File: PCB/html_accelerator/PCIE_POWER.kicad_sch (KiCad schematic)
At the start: 1 part, among them U1 MCS9990

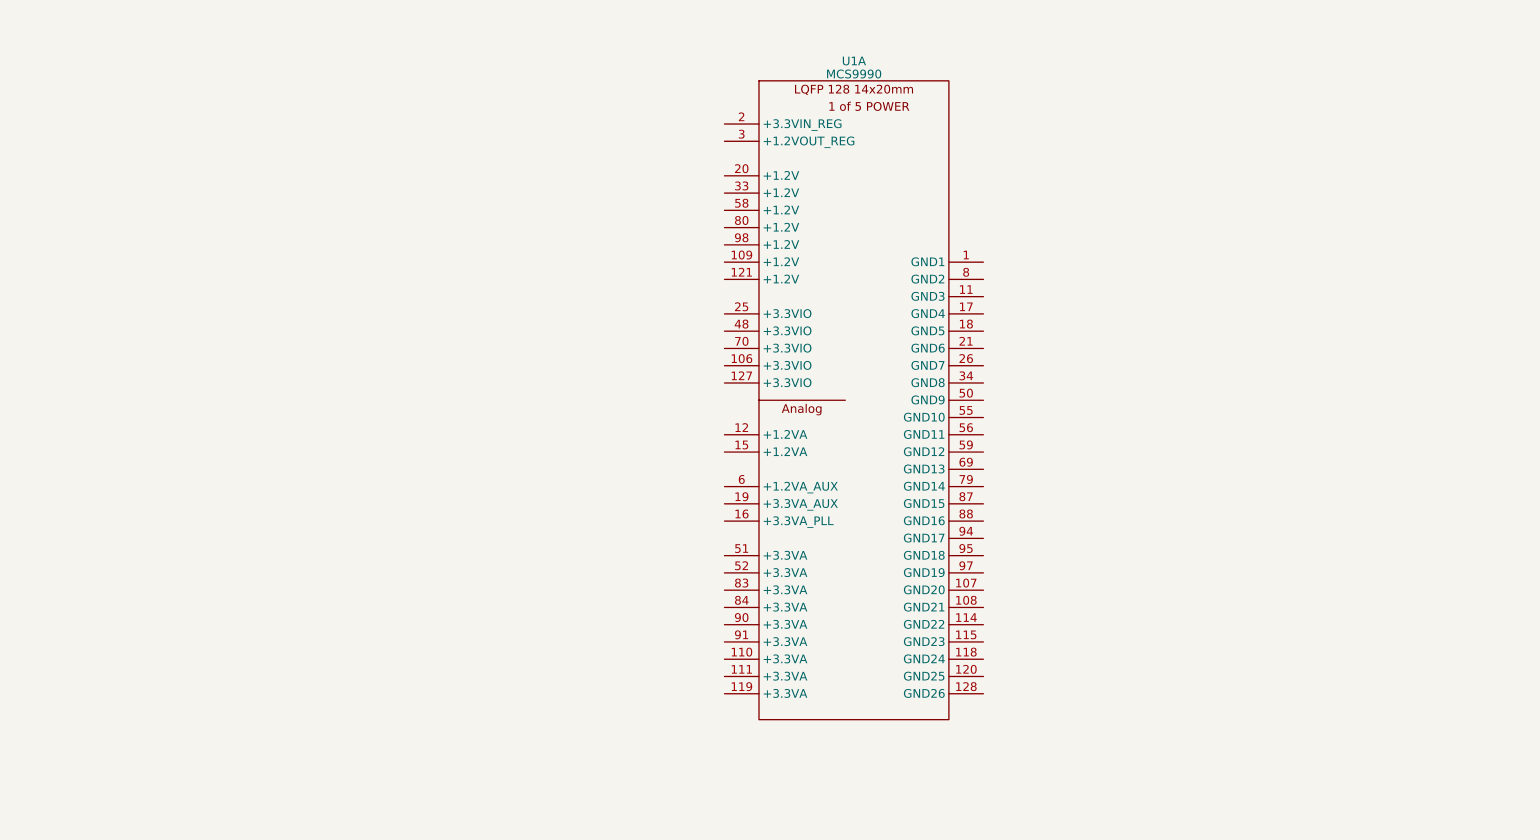
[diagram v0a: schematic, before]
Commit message: block diagram, datasheet updates
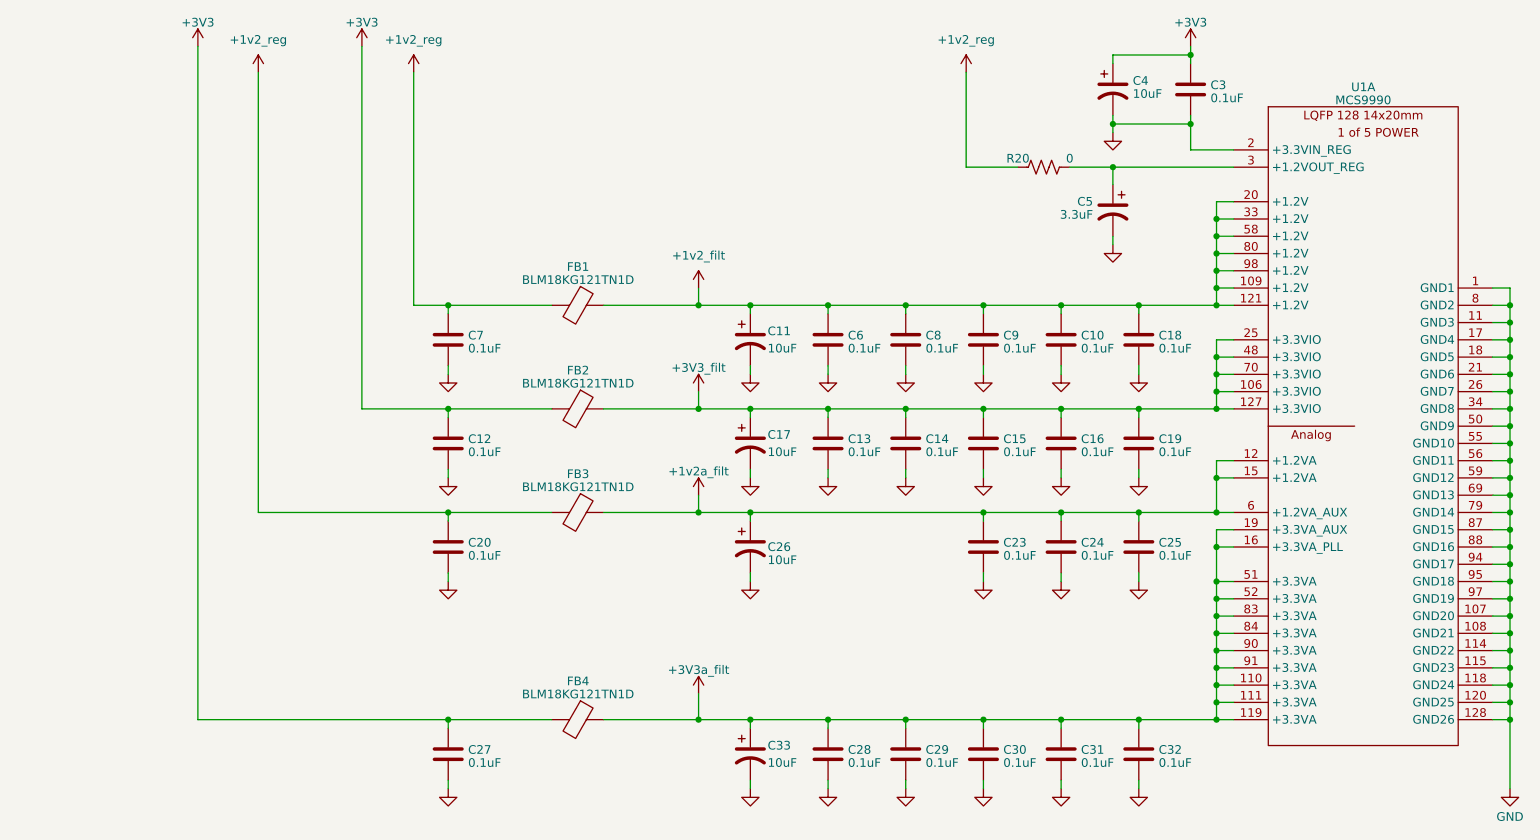
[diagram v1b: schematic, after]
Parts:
- added C10, C12, C13, C14, C15, C16, C18, C19, C20, C23, C24, C25, C27, C28, C29, C3, C30, C31, C32, C6, C7, C8, C9: 0.1uF, symbol Device:C
- added C11, C17, C26, C33, C4: 10uF, symbol Device:C_Polarized_US
- added C5: 3.3uF, symbol Device:C_Polarized_US
- added FB1, FB2, FB3, FB4: BLM18KG121TN1D, symbol Device:FerriteBead
- added R20: 0, symbol Device:R_US
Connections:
- net GND: now reaches U1.1 (GND1)
- net GND: now also U1.107 (GND20), U1.108 (GND21), U1.11 (GND3), U1.114 (GND22), U1.115 (GND23), U1.118 (GND24), U1.120 (GND25), U1.128 (GND26), U1.17 (GND4), U1.18 (GND5), U1.2 (+3.3VIN_REG), U1.21 (GND6), U1.26 (GND7), U1.34 (GND8), U1.50 (GND9), U1.55 (GND10), U1.56 (GND11), U1.59 (GND12), U1.69 (GND13), U1.79 (GND14), U1.8 (GND2), U1.87 (GND15), U1.88 (GND16), U1.94 (GND17), U1.95 (GND18), U1.97 (GND19), C10.2, C11.2, C12.2, C13.2, C14.2, C15.2, C16.2, C17.2, C18.2, C19.2, C20.2, C23.2, C24.2, C25.2, C26.2, C27.2, C28.2, C29.2, C3.2, C30.2, C31.2, C32.2, C33.2, C4.2, C5.2, C6.2, C7.2, C8.2, C9.2
- net +3V3: now reaches U1.106 (+3.3VIO)
- net +3V3: now also U1.109 (+1.2V), U1.110 (+3.3VA), U1.111 (+3.3VA), U1.119 (+3.3VA), U1.12 (+1.2VA), U1.121 (+1.2V), U1.127 (+3.3VIO), U1.15 (+1.2VA), U1.16 (+3.3VA_PLL), U1.19 (+3.3VA_AUX), U1.20 (+1.2V), U1.25 (+3.3VIO), U1.33 (+1.2V), U1.48 (+3.3VIO), U1.51 (+3.3VA), U1.52 (+3.3VA), U1.58 (+1.2V), U1.6 (+1.2VA_AUX), U1.70 (+3.3VIO), U1.80 (+1.2V), U1.83 (+3.3VA), U1.84 (+3.3VA), U1.90 (+3.3VA), U1.91 (+3.3VA), U1.98 (+1.2V), C10.1, C11.1, C12.1, C13.1, C14.1, C15.1, C16.1, C17.1, C18.1, C19.1, C20.1, C23.1, C24.1, C25.1, C26.1, C27.1, C28.1, C29.1, C3.1, C30.1, C31.1, C32.1, C33.1, C4.1, C6.1, C7.1, C8.1, C9.1, FB1.1, FB1.2, FB2.1, FB2.2, FB3.1, FB3.2, FB4.1, FB4.2, R20.1
- net at U1.3 (+1.2VOUT_REG): now also C5.1, R20.2
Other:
- moved on the sheet: U1A

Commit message: schematic updates
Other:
- title: (none) -> 12v, 3v3, 1v2 Power, Buck
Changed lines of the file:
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@@
 (kicad_sch (version 20230121) (generator eeschema)
   (paper "A4")
+  (title_block
+    (title "12v, 3v3, 1v2 Power, Buck")
+    (date "2024-09-15")
+    (rev "1")
+  )
   (junction (at 130.81 87.63) (diameter 0) (color 0 0 0 0)
   )
@@
   (symbol (lib_id "html_accel_Symbols:MCS9990") (at 207.01 43.18 0) (unit 1)
     (in_bom yes) (on_board yes) (dnp no) (fields_autoplaced)
-    (property "Reference" "U1" (at 220.98 40.2971 0)
-      (effects (font (size 1.27 1.27)))
+    (property "Reference" "U1" (at 220.98 38.8806 0)
+      (effects (font (size 3 3) bold))
     )
     (property "Value" "MCS9990" (at 220.98 42.2181 0)

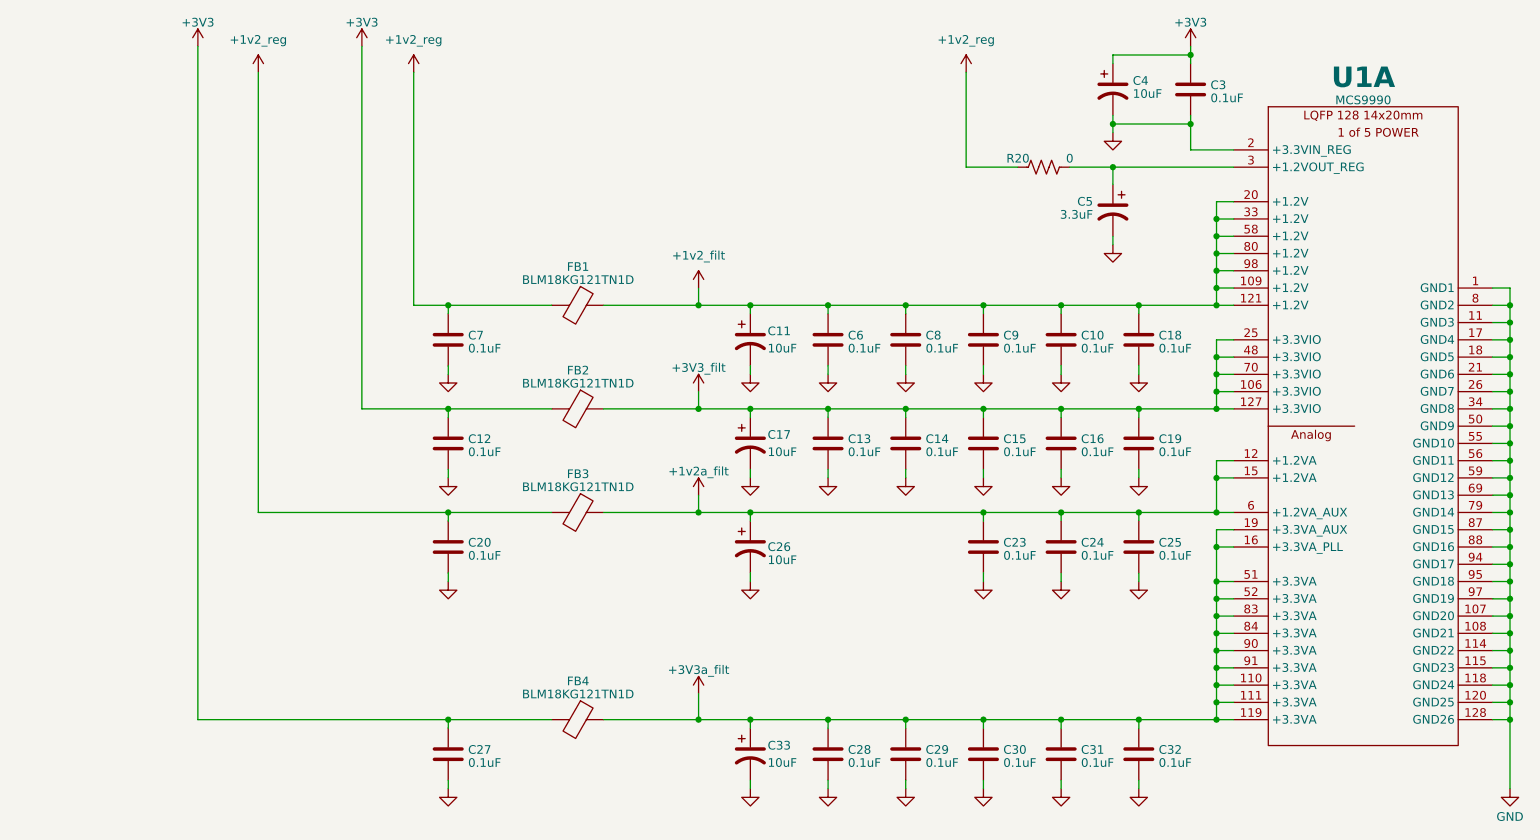
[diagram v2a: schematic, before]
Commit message: EMMC symbols and netlist
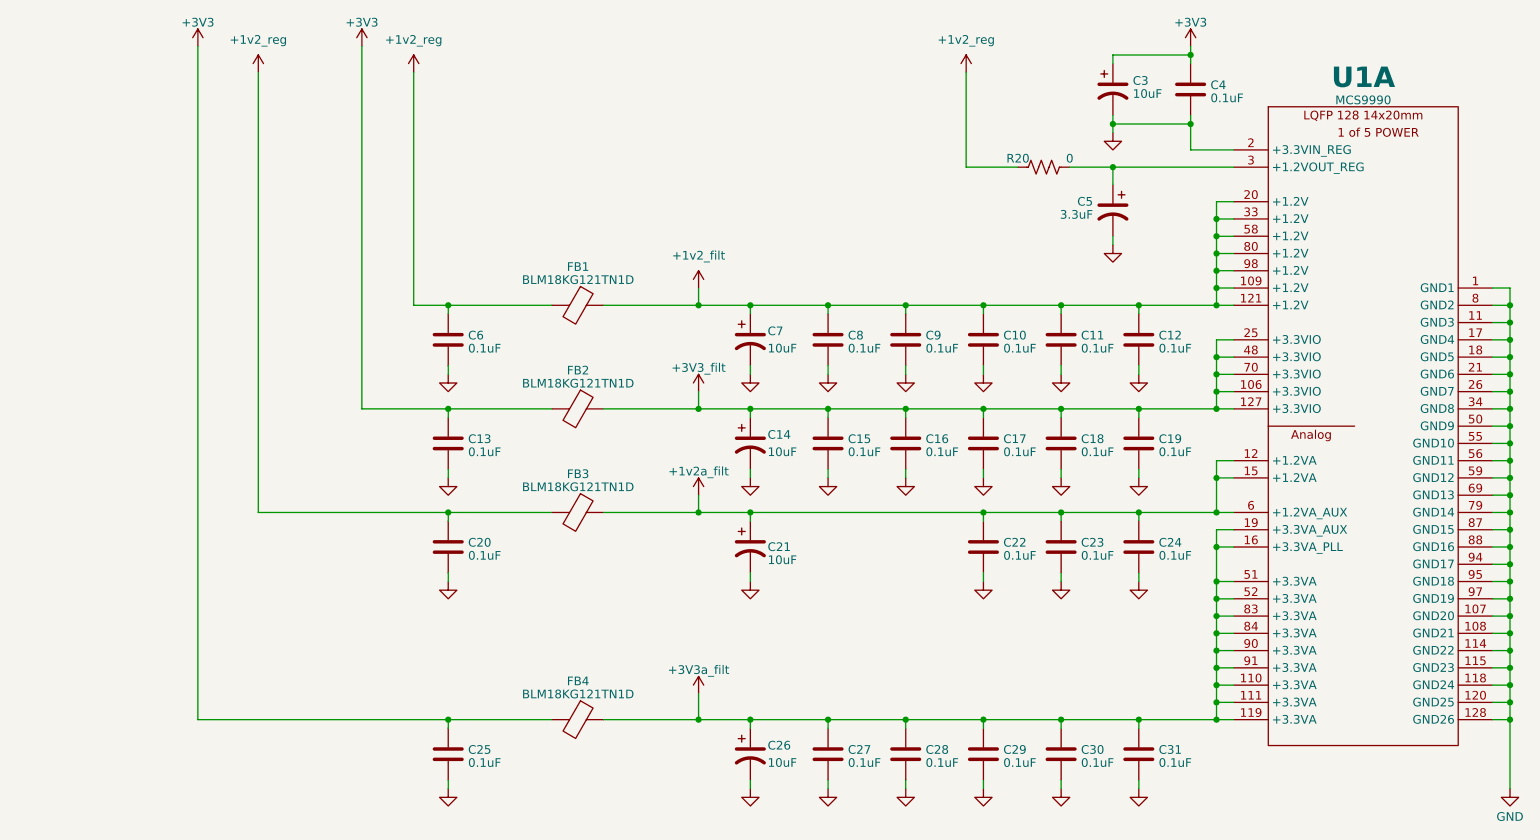
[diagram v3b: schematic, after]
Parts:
- renumbered C9 to C10, C10 to C11, C18 to C12, C12 to C13, C17 to C14, C13 to C15, C14 to C16, C15 to C17, C16 to C18, C26 to C21, C23 to C22, C24 to C23, C25 to C24, C27 to C25, C33 to C26, C28 to C27, C29 to C28, C30 to C29, C4 to C3, C31 to C30, C32 to C31, C3 to C4, C7 to C6, C11 to C7, C6 to C8, C8 to C9

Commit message: 3d part models, PCB netlist imported
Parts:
- C10, C11, C12, C13, C14, C15, C16, C17, C18, C19, C20, C21, C22, C23, C24, C25, C26, C27, C28, C29, C3, C30, C31, C4, C5, C6, C7, C8, C9: footprint (none) -> Capacitor_SMD:C_0805_2012Metric_Pad1.18x1.45mm_HandSolder
- FB1, FB2, FB3, FB4: value BLM18KG121TN1D -> BLM21PG121SN1D; footprint (none) -> Resistor_SMD:R_0805_2012Metric_Pad1.20x1.40mm_HandSolder
- R20: footprint (none) -> Resistor_SMD:R_0805_2012Metric_Pad1.20x1.40mm_HandSolder

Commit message: placement updates
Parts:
- removed C23, C24, C31: 0.1uF, Capacitor_SMD:C_0805_2012Metric_Pad1.18x1.45mm_HandSolder, symbol Device:C
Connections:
- net +3V3: now also U1.2 (+3.3VIN_REG); no longer C10.1, C11.1, C12.1, C14.1, C15.1, C16.1, C17.1, C18.1, C19.1, C20.1, C21.1, C22.1, C26.1, C27.1, C28.1, C29.1, C30.1, C6.1, C7.1, C8.1, C9.1, FB1.1, FB1.2, FB2.1, FB3.1, FB3.2, FB4.1, R20.1, U1.106 (+3.3VIO), U1.109 (+1.2V), U1.110 (+3.3VA), U1.111 (+3.3VA), U1.119 (+3.3VA), U1.12 (+1.2VA), U1.121 (+1.2V), U1.127 (+3.3VIO), U1.15 (+1.2VA), U1.16 (+3.3VA_PLL), U1.19 (+3.3VA_AUX), U1.20 (+1.2V), U1.25 (+3.3VIO), U1.33 (+1.2V), U1.48 (+3.3VIO), U1.51 (+3.3VA), U1.52 (+3.3VA), U1.58 (+1.2V), U1.6 (+1.2VA_AUX), U1.70 (+3.3VIO), U1.80 (+1.2V), U1.83 (+3.3VA), U1.84 (+3.3VA), U1.90 (+3.3VA), U1.91 (+3.3VA), U1.98 (+1.2V)
- net GND: no longer U1.2 (+3.3VIN_REG)
- new net: C26.1, C27.1, C28.1, C29.1, C30.1, FB4.1, U1.110 (+3.3VA), U1.111 (+3.3VA), U1.119 (+3.3VA), U1.16 (+3.3VA_PLL), U1.19 (+3.3VA_AUX), U1.51 (+3.3VA), U1.52 (+3.3VA), U1.83 (+3.3VA), U1.84 (+3.3VA), U1.90 (+3.3VA), U1.91 (+3.3VA)
- new net: C10.1, C11.1, C12.1, C7.1, C8.1, C9.1, FB1.1, U1.109 (+1.2V), U1.121 (+1.2V), U1.20 (+1.2V), U1.33 (+1.2V), U1.58 (+1.2V), U1.80 (+1.2V), U1.98 (+1.2V)
- new net: C21.1, C22.1, FB3.1, U1.12 (+1.2VA), U1.15 (+1.2VA), U1.6 (+1.2VA_AUX)
- new net +1V2: C20.1, C6.1, FB1.2, FB3.2, R20.1
- new net 3v3_filt: C14.1, C15.1, C16.1, C17.1, C18.1, C19.1, FB2.1, U1.106 (+3.3VIO), U1.127 (+3.3VIO), U1.25 (+3.3VIO), U1.48 (+3.3VIO), U1.70 (+3.3VIO)
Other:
- moved on the sheet: C13, C20, C25, C3, C4, C6, FB1, FB2, FB3, FB4

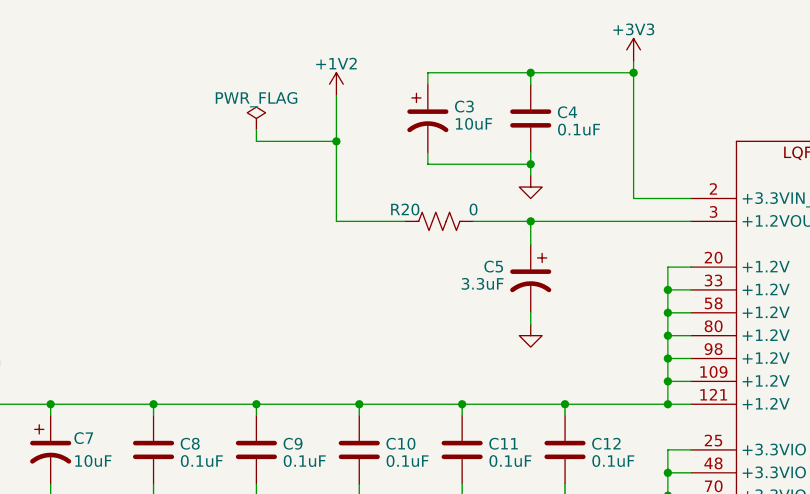
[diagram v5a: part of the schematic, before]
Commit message: constraints for impedance control
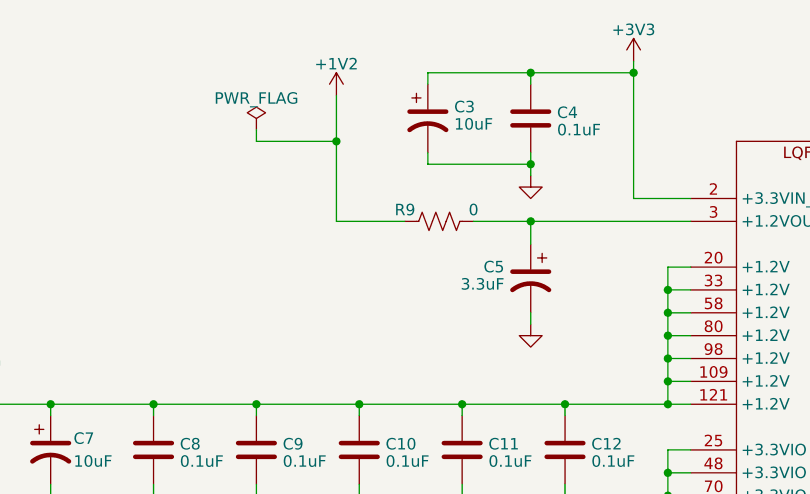
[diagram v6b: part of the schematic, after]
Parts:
- renumbered R20 to R9
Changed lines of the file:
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@@
   (symbol (lib_id "Device:R_US") (at 173.99 52.07 90) (unit 1)
     (in_bom yes) (on_board yes) (dnp no)
-    (property "Reference" "R20" (at 170.18 50.8 90)
+    (property "Reference" "R9" (at 170.18 50.8 90)
       (effects (font (size 1.27 1.27)))
     )
@@
     (instances
       (project "html_accelerator"
-        (path "/12b3a7c9-141f-40ba-9ebb-094b58bfa6c7/3421334e-11b3-46c8-b0f2-353f0fa6f362"
-          (reference "R20") (unit 1)
-        )
         (path "/12b3a7c9-141f-40ba-9ebb-094b58bfa6c7/8c9bd1fc-c6d3-45cd-babe-9d9e8ea6549d"
           (reference "R9") (unit 1)
@@
     (instances
       (project "html_accelerator"
-        (path "/12b3a7c9-141f-40ba-9ebb-094b58bfa6c7/3421334e-11b3-46c8-b0f2-353f0fa6f362"
-          (reference "U1") (unit 1)
-        )
         (path "/12b3a7c9-141f-40ba-9ebb-094b58bfa6c7/8c9bd1fc-c6d3-45cd-babe-9d9e8ea6549d"
           (reference "U1") (unit 1)

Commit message: routing checkpoint
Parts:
- removed C20, C25: 0.1uF, Capacitor_SMD:C_0805_2012Metric_Pad1.18x1.45mm_HandSolder, symbol Device:C
- removed FB3, FB4: BLM21PG121SN1D, Resistor_SMD:R_0805_2012Metric_Pad1.20x1.40mm_HandSolder, symbol Device:FerriteBead
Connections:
- net 3v3_filt: now also C26.1, C27.1, C28.1, C29.1, C30.1, U1.110 (+3.3VA), U1.111 (+3.3VA), U1.119 (+3.3VA), U1.16 (+3.3VA_PLL), U1.19 (+3.3VA_AUX), U1.51 (+3.3VA), U1.52 (+3.3VA), U1.83 (+3.3VA), U1.84 (+3.3VA), U1.90 (+3.3VA), U1.91 (+3.3VA)
- net 1v2_filt: now reaches C10.1, C11.1, C12.1, C7.1, C8.1, C9.1, FB1.1, U1.109 (+1.2V), U1.121 (+1.2V), U1.20 (+1.2V), U1.33 (+1.2V), U1.58 (+1.2V), U1.80 (+1.2V), U1.98 (+1.2V)
- net 1v2_filt: now also C21.1, C22.1, U1.12 (+1.2VA), U1.15 (+1.2VA), U1.6 (+1.2VA_AUX)
- net 1v2_REG: now reaches C5.1, R9.2, U1.3 (+1.2VOUT_REG)
